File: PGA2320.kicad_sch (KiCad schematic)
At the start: 39 parts, among them J1 XH2.54-3P, J2 XH2.54-3P, J3 2P-2.54, J4 3P-2.54, P1 SDO_TO_OTHER_PGA2311, P2 CONTROLLER, Q1 BC550, Q2 BC560, U1 PGA2320

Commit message: improvements
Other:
- added sheet MCU_ATMEGA32U4 (ATMEGA32U4.kicad_sch)
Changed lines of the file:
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@@
+    )
+  )
+  (sheet (at 71.12 101.6) (size 45.72 21.59) (fields_autoplaced)
+    (stroke (width 0.1524) (type solid))
+    (fill (color 0 0 0 0.0000))
+    (property "Sheetname" "MCU_ATMEGA32U4" (at 71.12 100.8884 0)
+      (effects (font (size 1.27 1.27)) (justify left bottom))
+    )
+    (property "Sheetfile" "ATMEGA32U4.kicad_sch" (at 71.12 123.7746 0)
+      (effects (font (size 1.27 1.27)) (justify left top))
+    )
+    (instances
+      (project "PGA2320"
+        (path "/3c367401-208f-4628-9cce-4b3b1ae65d20" (page "2"))
+      )
     )
   )

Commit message: improvements
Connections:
- net +15V: now also R2.1
- net +16V to +18V: no longer R2.1
- net -15V: now also D3.1 (K)
- net -16V to -18V: no longer D3.1 (K)
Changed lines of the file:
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@@
     (stroke (width 0) (type default))
   )
-  (wire (pts (xy 30.48 66.04) (xy 43.18 66.04))
+  (wire (pts (xy 40.64 66.04) (xy 43.18 66.04))
     (stroke (width 0) (type default))
   )
@@
     (stroke (width 0) (type default))
   )
-  (polyline (pts (xy 30.48 48.26) (xy 41.91 48.26))
+  (polyline (pts (xy 29.21 48.26) (xy 41.91 48.26))
     (stroke (width 0) (type default))
   )
@@
     (stroke (width 0) (type default))
   )
-  (polyline (pts (xy 30.48 83.82) (xy 30.48 48.26))
+  (polyline (pts (xy 29.21 83.82) (xy 29.21 48.26))
     (stroke (width 0) (type default))
   )
@@
     (stroke (width 0) (type default))
   )
-  (polyline (pts (xy 74.93 83.82) (xy 30.48 83.82))
+  (polyline (pts (xy 74.93 83.82) (xy 29.21 83.82))
     (stroke (width 0) (type default))
   )
@@
     (effects (font (size 1.27 1.27)) (justify left bottom))
   )
-  (label "-16V to -18V" (at 64.77 77.47 0) (fields_autoplaced)
-    (effects (font (size 1.27 1.27)) (justify left bottom))
-  )
   (label "GND_A" (at 252.73 114.3 0) (fields_autoplaced)
     (effects (font (size 1.27 1.27)) (justify left bottom))
   )
-  (label "+16V to +18V" (at 30.48 66.04 0) (fields_autoplaced)
-    (effects (font (size 1.27 1.27)) (justify left bottom))
-  )
   (label "GND_A" (at 21.59 194.31 0) (fields_autoplaced)
     (effects (font (size 1.27 1.27)) (justify left bottom))
@@
     )
   )
+  (global_label "-15V" (shape input) (at 64.77 77.47 0) (fields_autoplaced)
+    (effects (font (size 1.524 1.524)) (justify left))
+    (property "Intersheetrefs" "${INTERSHEET_REFS}" (at 74.4477 77.47 0)
+      (effects (font (size 1.524 1.524)) (justify left) hide)
+    )
+  )
   (global_label "-15V" (shape output) (at 139.7 170.18 0) (fields_autoplaced)
     (effects (font (size 1.524 1.524)) (justify left))
@@
     )
   )
+  (global_label "+15V" (shape input) (at 40.64 66.04 180) (fields_autoplaced)
+    (effects (font (size 1.524 1.524)) (justify right))
+    (property "Intersheetrefs" "${INTERSHEET_REFS}" (at 30.9623 66.04 0)
+      (effects (font (size 1.524 1.524)) (justify right) hide)
+    )
+  )

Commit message: improvements
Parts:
- added C21: 0.1uf, Audio_Module:c_0805, symbol Device:C_Small
- added C22: 10uf, Audio_Module:c_tant_C, symbol Device:C_Small
- added U3: MIC5219-3_3YM5-TR, digikey-footprints:SOT-753, symbol dk_PMIC-Voltage-Regulators-Linear:MIC5219-3_3YM5-TR
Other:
- moved on the sheet: D1, D2, D3, JP1, R1, R2, R3

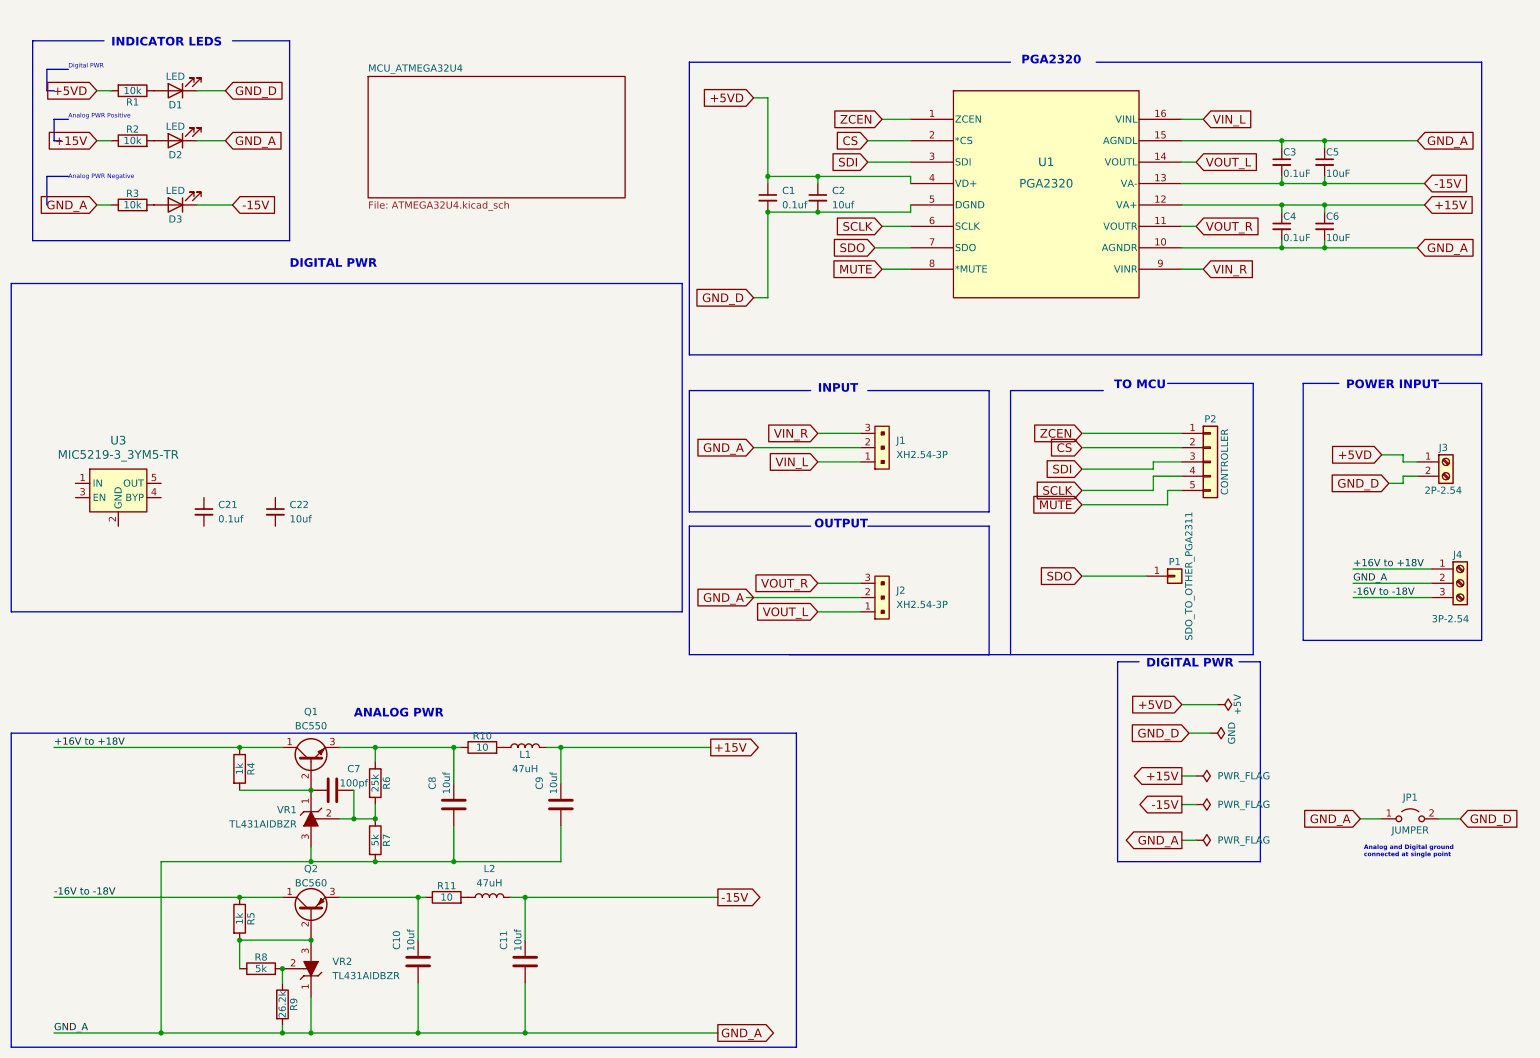
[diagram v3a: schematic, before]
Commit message: add power supply for vdd
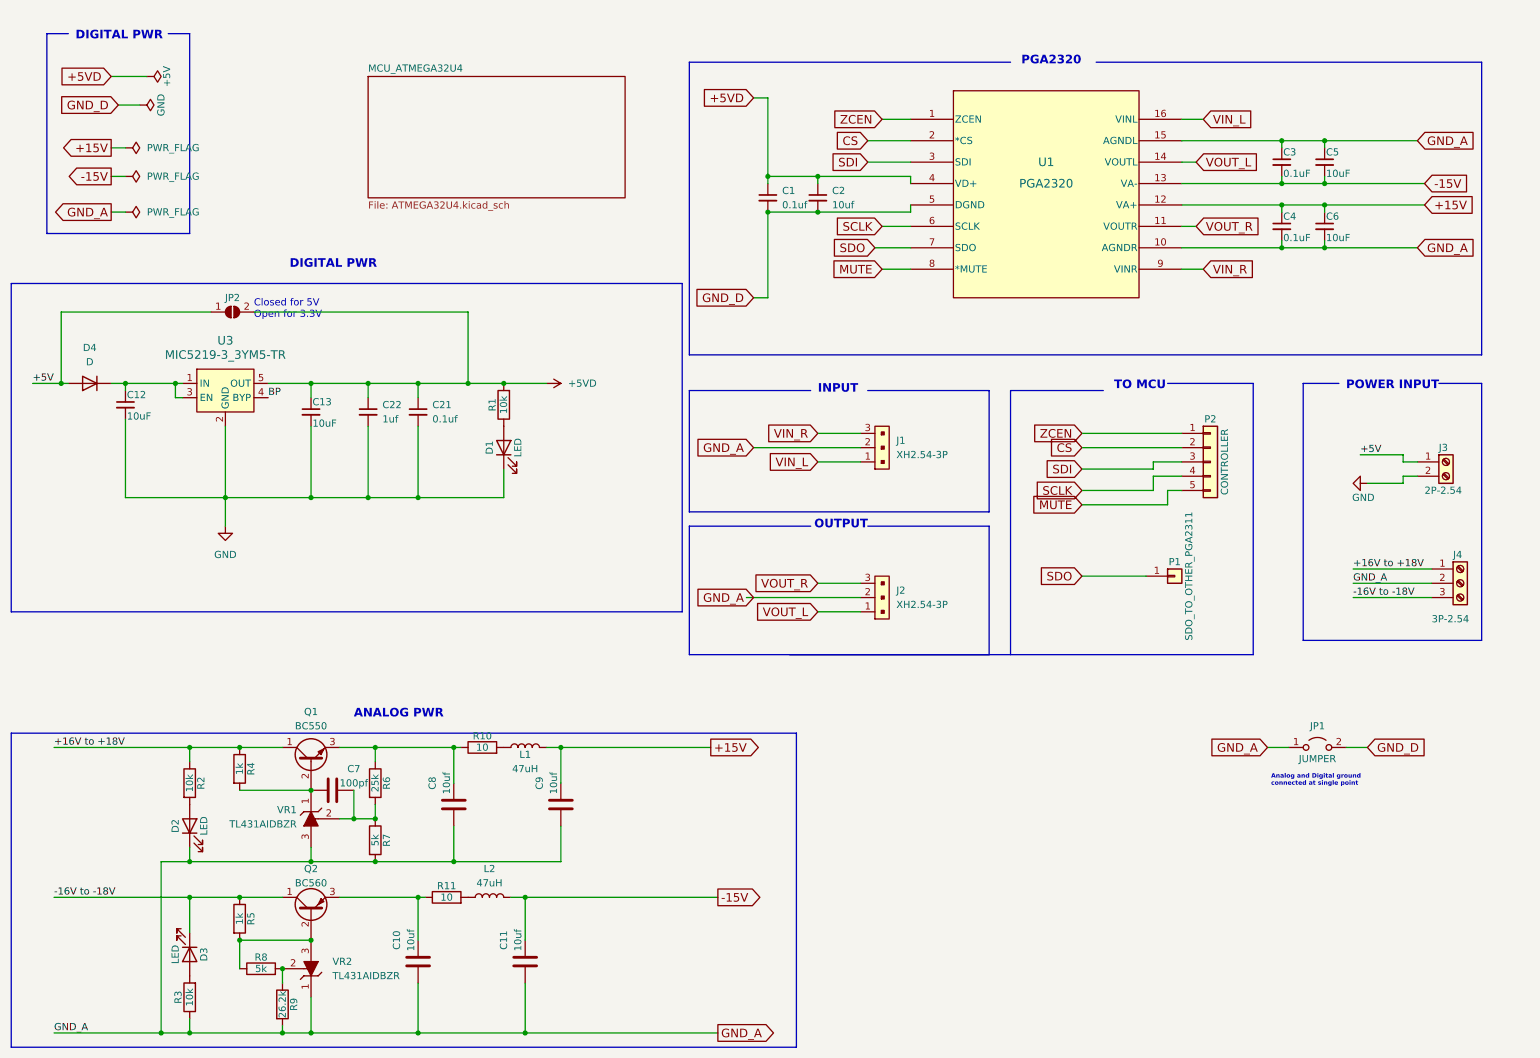
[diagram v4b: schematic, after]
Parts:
- added C12, C13: 10uF, Audio_Module:c_tant_C, symbol Device:C_Small
- added D4: D, Diode_SMD:D_0805_2012Metric, symbol Device:D
- added JP2: SolderJumper_2_Open, symbol Jumper:SolderJumper_2_Open
- C21: footprint Audio_Module:c_0805 -> Capacitor_SMD:C_0805_2012Metric
- C22: value 10uf -> 1uf; footprint Audio_Module:c_tant_C -> Capacitor_SMD:C_0805_2012Metric
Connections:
- net +15V: no longer R2.1
- net +16V to +18V: now also R2.1
- net +5VD: now also C21.1, C22.1, U3.5 (OUT), C13.1, JP2.2 (B); no longer J3.1 (Pin_1)
- net -15V: no longer D3.1 (K)
- net -16V to -18V: now also D3.1 (K)
- net GND_D: no longer D1.1 (K), J3.2 (Pin_2)
- net GND: now reaches C21.2
- net GND: now also C22.2, D1.1 (K), J3.2 (Pin_2), U3.2 (GND), C12.2, C13.2
- net at U3.1 (IN): now also U3.3 (EN), C12.1, D4.1 (K)
- net BP: now reaches U3.4 (BYP)
- new net +5V: D4.2 (A), J3.1 (Pin_1), JP2.1 (A)
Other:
- note added: "Closed for 5V Open for 3.3V"
- note removed: "Analog PWR Negative"
- note removed: "Analog PWR Positive"
- note removed: "Digital PWR"
- note removed: "INDICATOR LEDS"
- moved on the sheet: C21, C22, D2, JP1, R2, U3

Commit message: scheme
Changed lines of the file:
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@@
     (stroke (width 0) (type default))
   )
-  (polyline (pts (xy 45.72 52.07) (xy 20.32 52.07))
-    (stroke (width 0) (type default))
-  )
-  (polyline (pts (xy 20.32 52.07) (xy 20.32 16.51))
+  (polyline (pts (xy 50.8 52.07) (xy 15.24 52.07))
+    (stroke (width 0) (type default))
+  )
+  (polyline (pts (xy 15.24 52.07) (xy 15.24 13.97))
     (stroke (width 0) (type default))
   )
@@
     (stroke (width 0) (type default))
   )
-  (wire (pts (xy 31.75 24.13) (xy 38.1 24.13))
+  (wire (pts (xy 31.75 24.13) (xy 36.83 24.13))
     (stroke (width 0) (type default))
   )
@@
     (stroke (width 0) (type default))
   )
-  (polyline (pts (xy 20.32 16.51) (xy 24.13 16.51))
+  (polyline (pts (xy 15.24 13.97) (xy 24.13 13.97))
     (stroke (width 0) (type default))
   )
@@
     (stroke (width 0) (type default))
   )
-  (polyline (pts (xy 45.72 16.51) (xy 45.72 52.07))
+  (polyline (pts (xy 50.8 13.97) (xy 50.8 52.07))
     (stroke (width 0) (type default))
   )
@@
     (stroke (width 0) (type default))
   )
+  (wire (pts (xy 30.48 16.51) (xy 36.83 16.51))
+    (stroke (width 0) (type default))
+  )
   (wire (pts (xy 92.71 149.86) (xy 92.71 143.51))
     (stroke (width 0) (type default))
@@
     (stroke (width 0) (type default))
   )
-  (polyline (pts (xy 41.91 16.51) (xy 45.72 16.51))
+  (polyline (pts (xy 41.91 13.97) (xy 50.8 13.97))
     (stroke (width 0) (type default))
   )
@@
     (effects (font (size 1.524 1.524) (thickness 0.3048) bold) (justify left bottom))
   )
-  (text "DIGITAL PWR" (at 25.4 17.78 0)
+  (text "DIGITAL PWR" (at 25.4 15.24 0)
     (effects (font (size 1.524 1.524) (thickness 0.3048) bold) (justify left bottom))
   )
@@
     )
   )
-  (symbol (lib_id "power:PWR_FLAG") (at 38.1 24.13 270) (unit 1)
-    (in_bom yes) (on_board yes) (dnp no)
-    (property "Reference" "#PWR03" (at 34.29 24.13 0)
-      (effects (font (size 1.27 1.27)) hide)
-    )
-    (property "Value" "+5V" (at 41.656 24.13 0)
-      (effects (font (size 1.27 1.27)))
-    )
-    (property "Footprint" "" (at 38.1 24.13 0)
-      (effects (font (size 1.27 1.27)) hide)
-    )
-    (property "Datasheet" "~" (at 38.1 24.13 0)
-      (effects (font (size 1.27 1.27)) hide)
-    )
-    (pin "1")
-    (instances
-      (project "PGA2320"
-        (path "/3c367401-208f-4628-9cce-4b3b1ae65d20"
-          (reference "#PWR03") (unit 1)
-        )
-      )
-      (project "pga2311"
-        (path "/5b7801f4-55a7-4c74-b3bf-bacecbb4cf6a"
-          (reference "#PWR07") (unit 1)
+  (symbol (lib_id "power:PWR_FLAG") (at 36.83 24.13 270) (unit 1)
+    (in_bom yes) (on_board yes) (dnp no) (fields_autoplaced)
+    (property "Reference" "#FLG04" (at 38.735 24.13 0)
+      (effects (font (size 1.27 1.27)) hide)
+    )
+    (property "Value" "PWR_FLAG" (at 40.64 24.13 90)
+      (effects (font (size 1.27 1.27)) (justify left))
+    )
+    (property "Footprint" "" (at 36.83 24.13 0)
+      (effects (font (size 1.27 1.27)) hide)
+    )
+    (property "Datasheet" "~" (at 36.83 24.13 0)
+      (effects (font (size 1.27 1.27)) hide)
+    )
+    (pin "1")
+    (instances
+      (project "PGA2320"
+        (path "/3c367401-208f-4628-9cce-4b3b1ae65d20"
+          (reference "#FLG04") (unit 1)
         )
       )
@@
     )
   )
+  (symbol (lib_id "power:PWR_FLAG") (at 36.83 16.51 270) (unit 1)
+    (in_bom yes) (on_board yes) (dnp no) (fields_autoplaced)
+    (property "Reference" "#FLG05" (at 38.735 16.51 0)
+      (effects (font (size 1.27 1.27)) hide)
+    )
+    (property "Value" "PWR_FLAG" (at 40.64 16.51 90)
+      (effects (font (size 1.27 1.27)) (justify left))
+    )
+    (property "Footprint" "" (at 36.83 16.51 0)
+      (effects (font (size 1.27 1.27)) hide)
+    )
+    (property "Datasheet" "~" (at 36.83 16.51 0)
+      (effects (font (size 1.27 1.27)) hide)
+    )
+    (pin "1")
+    (instances
+      (project "PGA2320"
+        (path "/3c367401-208f-4628-9cce-4b3b1ae65d20"
+          (reference "#FLG05") (unit 1)
+        )
+      )
+    )
+  )
   (symbol (lib_id "Device:LED") (at 45.72 157.48 90) (unit 1)
     (in_bom yes) (on_board yes) (dnp no)
@@
         )
       )
+    )
+  )
+  (symbol (lib_id "PCM_4ms_Power-symbol:GND") (at 30.48 16.51 270) (unit 1)
+    (in_bom yes) (on_board yes) (dnp no) (fields_autoplaced)
+    (property "Reference" "#PWR03" (at 24.13 16.51 0)
+      (effects (font (size 1.27 1.27)) hide)
+    )
+    (property "Value" "GND" (at 26.67 16.51 90)
+      (effects (font (size 1.27 1.27)) (justify right))
+    )
+    (property "Footprint" "" (at 30.48 16.51 0)
+      (effects (font (size 1.27 1.27)) hide)
+    )
+    (property "Datasheet" "" (at 30.48 16.51 0)
+      (effects (font (size 1.27 1.27)) hide)
+    )
+    (pin "1")
+    (instances
+      (project "PGA2320"
+        (path "/3c367401-208f-4628-9cce-4b3b1ae65d20"
+          (reference "#PWR03") (unit 1)
+        )
+      )
